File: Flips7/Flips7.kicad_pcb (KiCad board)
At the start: 2 copper layers, 100 x 100 mm, 14 parts, among them U1 FP2800A, U2 FP2800A, U3 FP2800A

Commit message: tracing flips7
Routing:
- net /YR09: track 1.91 -> 128.8 mm, vias 0 -> 1
- net /YR08: track 0.00 -> 123.7 mm, vias 0 -> 1
- net /YS09: track 0.00 -> 118.6 mm, vias 0 -> 2
- net /YS05: track 0.00 -> 118.6 mm, vias 0 -> 1
- net /YS01: track 0.00 -> 116.1 mm, vias 0 -> 1
- net /YS04: track 0.00 -> 115.7 mm, vias 0 -> 1
- net /YR11: track 4.97 -> 120.4 mm, vias 0 -> 1
- net /YS08: track 0.00 -> 113.6 mm, vias 0 -> 1
- net /YS11: track 4.97 -> 115.4 mm, vias 0 -> 1
- net /YS16: track 4.97 -> 105.9 mm, vias 0 -> 3
- net /YS02: track 0.00 -> 98.3 mm, vias 0 -> 1
- net /X01: track 4.97 -> 102.1 mm, vias 0 -> 3
- net /X03: track 4.97 -> 102.1 mm, vias 0 -> 3
- net /X02: track 4.97 -> 101.4 mm, vias 0 -> 3
- net /YR05: track 0.00 -> 95.8 mm, vias 0 -> 1
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- added copper zone on F.Cu, net /X.GND
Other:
- net class Default: via_dia 0.8 -> 0.6; via_drill 0.4 -> 0.3
- net class POW: via_dia 0.8 -> 0.6; via_drill 0.4 -> 0.3

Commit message: adding row driver share connectors
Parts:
- added CN1: Conn_02x16_Odd_Even, Pin_Headers:Pin_Header_Straight_2x16_Pitch2.54mm, F.Cu at (73.0, 57.1)
- added CN2: Conn_02x16_Odd_Even, Pin_Headers:Pin_Header_Straight_2x16_Pitch2.54mm, F.Cu at (125.1, 57.1)
- moved BOARD1 24.1 mm to (77.5, 82.5)
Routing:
- net /YR12: track 67.8 -> 162.1 mm, vias 1 -> 4
- net /YS12: track 56.4 -> 147.2 mm, vias 0 -> 3
- net /YR13: track 65.3 -> 150.7 mm, vias 1 -> 4
- net /YR14: track 75.8 -> 156.0 mm, vias 1 -> 4
- net /YR16: track 79.3 -> 158.9 mm, vias 3 -> 6
- net /YR09: track 128.8 -> 208.4 mm, vias 1 -> 4
- net /YR15: track 79.3 -> 157.7 mm, vias 3 -> 6
- net /YR07: track 55.9 -> 134.2 mm, vias 1 -> 4
- net /YS13: track 62.0 -> 138.8 mm, vias 1 -> 4
- net /YS07: track 62.8 -> 136.3 mm, vias 1 -> 4
- net /YR11: track 120.4 -> 193.8 mm, vias 1 -> 4
- net /YR08: track 123.7 -> 196.9 mm, vias 1 -> 4
- net /YS14: track 93.2 -> 166.2 mm, vias 1 -> 4
- net /YS16: track 105.9 -> 178.3 mm, vias 3 -> 6
- net /YS15: track 95.8 -> 166.9 mm, vias 3 -> 6
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
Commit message: optimize routing
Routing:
- net /YS09: track 187.1 -> 144.6 mm
- net /X02: track 77.6 -> 93.7 mm
- net /X03: track 78.0 -> 90.7 mm
- net /YS16: track 178.3 -> 171.2 mm, vias 6 -> 4
- net /YS15: track 166.9 -> 162.3 mm, vias 6 -> 4
- net /X12: track 57.1 -> 54.0 mm, vias 3 -> 2
- net /YR07: track 134.2 -> 131.1 mm
- net /YR14: track 156.0 -> 154.2 mm
- net /YR13: track 150.7 -> 148.9 mm
- net /YR12: track 162.1 -> 160.3 mm
- net /YR11: track 193.8 -> 192.0 mm
- net /YR09: track 208.4 -> 206.6 mm
- net /YR08: track 196.9 -> 195.1 mm
- net /YR05: track 165.2 -> 163.4 mm
- net /YR04: track 140.4 -> 138.6 mm
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
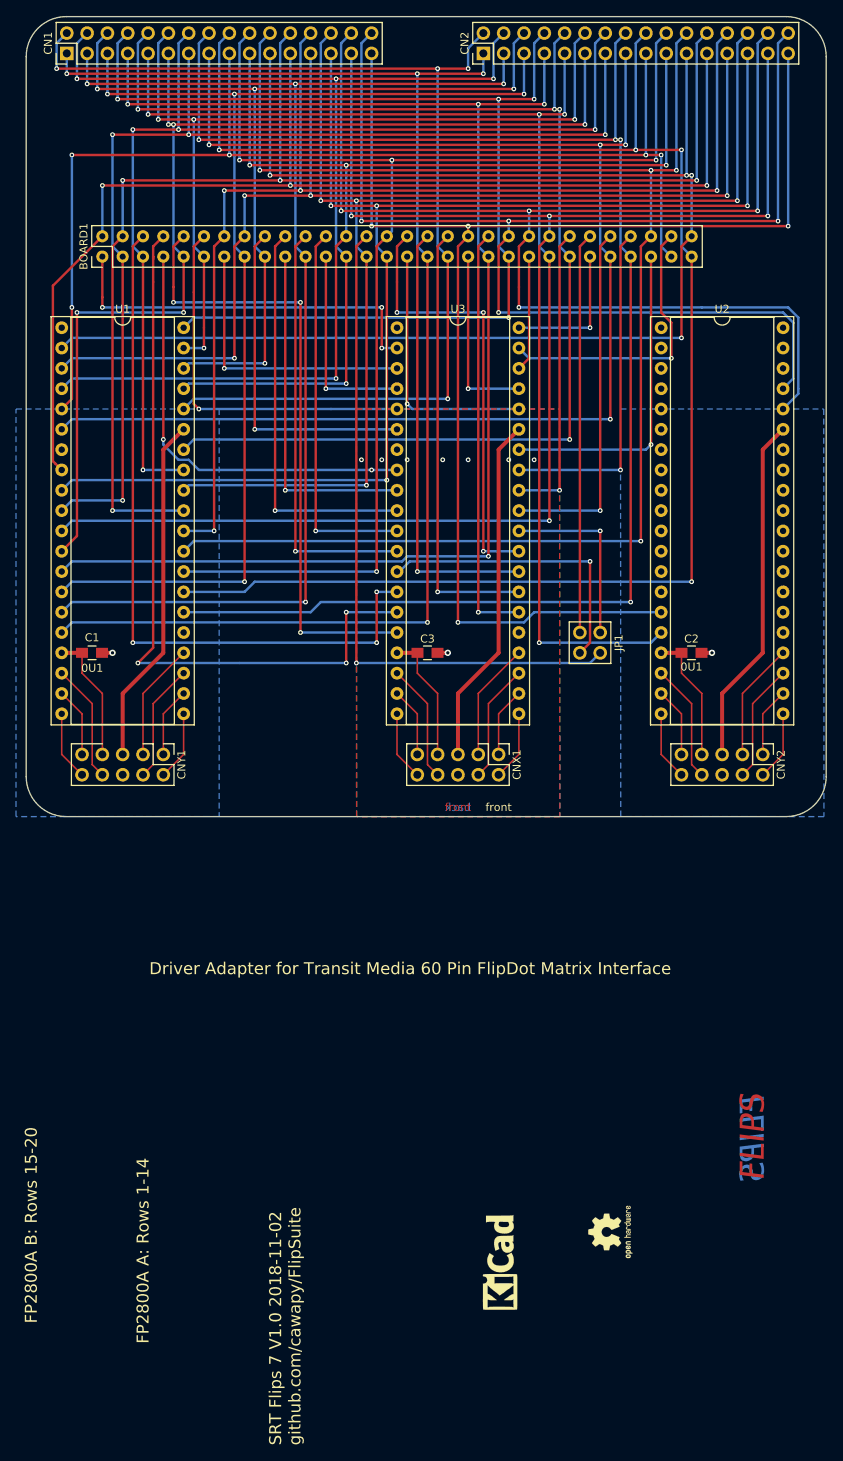
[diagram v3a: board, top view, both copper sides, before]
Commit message: more re-routing
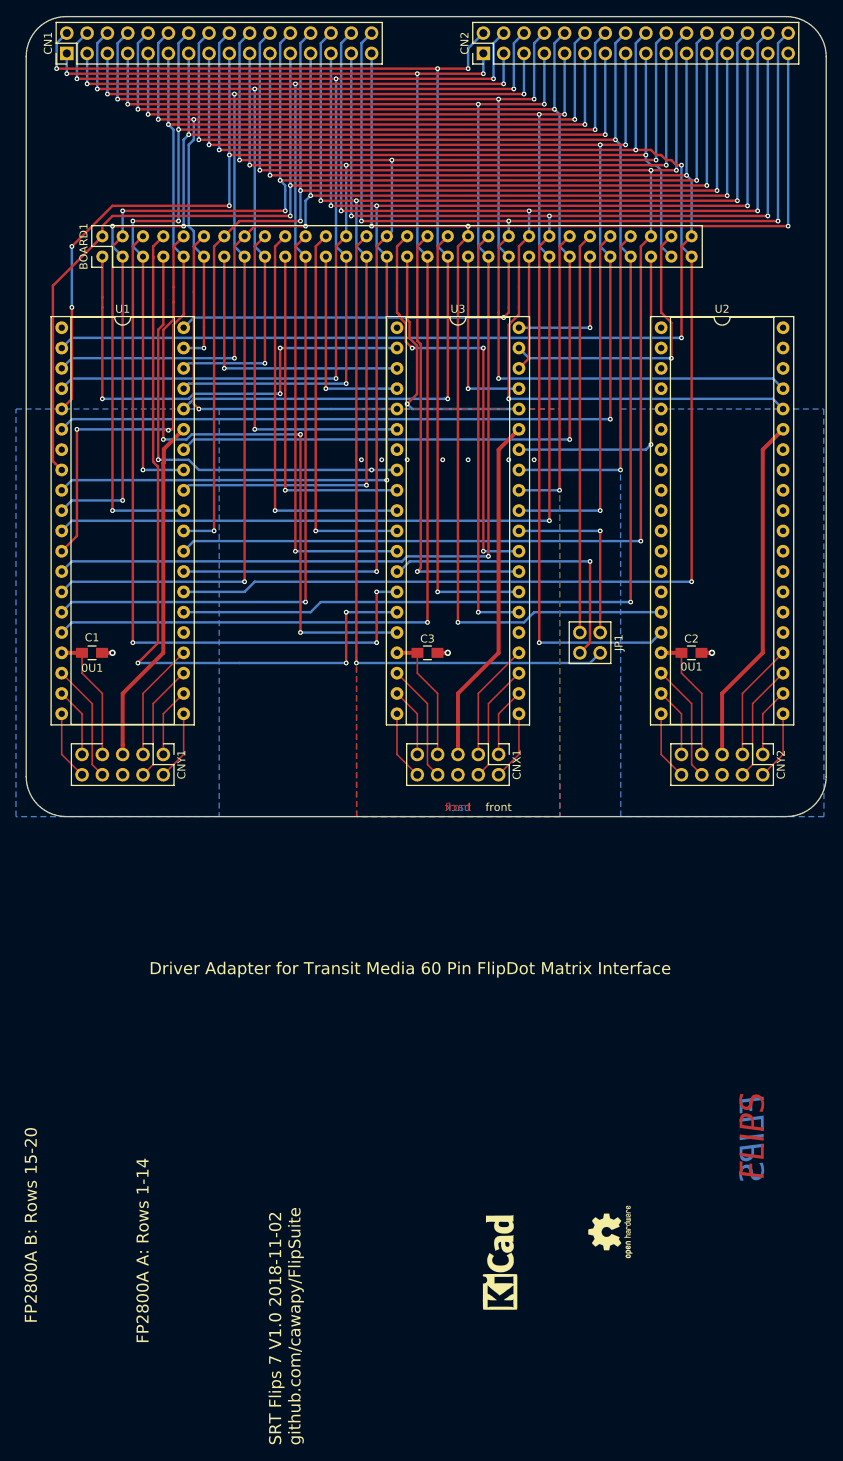
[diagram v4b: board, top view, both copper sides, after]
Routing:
- net /X11: track 48.3 -> 60.6 mm
- net /YS09: track 144.6 -> 140.8 mm
- net /X01: track 78.0 -> 80.7 mm
- net /X12: track 54.0 -> 56.0 mm
- net /YR16: track 158.2 -> 156.4 mm
- net /YS13: track 138.8 -> 137.7 mm
- net /YR09: track 206.6 -> 205.5 mm
- net /X25: track 55.1 -> 54.0 mm
- net /YR13: track 148.9 -> 147.8 mm
- net /X15: track 32.6 -> 33.7 mm
- net /YR15: track 157.8 -> 156.9 mm
- net /YR12: track 160.3 -> 161.2 mm, vias 4 -> 5
- net /YS12: track 147.2 -> 146.4 mm
- net /YR06: track 106.4 -> 106.9 mm
- net /X02: track 93.7 -> 94.2 mm
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
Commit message: rename row pins to /SY## and RY##
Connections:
- net /YR01 renamed /RY01
- net /YR02 renamed /RY02
- net /YR03 renamed /RY03
- net /YR04 renamed /RY04
- net /YR05 renamed /RY05
- net /YR06 renamed /RY06
- net /YR07 renamed /RY07
- net /YR08 renamed /RY08
- net /YR09 renamed /RY09
- net /YR10 renamed /RY10
- net /YR11 renamed /RY11
- net /YR12 renamed /RY12
- net /YR13 renamed /RY13
- net /YR14 renamed /RY14
- net /YR15 renamed /RY15
- net /YR16 renamed /RY16
- net /YS01 renamed /~SY01
- net /YS02 renamed /~SY02
- net /YS03 renamed /~SY03
- net /YS04 renamed /~SY04
- net /YS05 renamed /~SY05
- net /YS06 renamed /~SY06
- net /YS07 renamed /~SY07
- net /YS08 renamed /~SY08
- net /YS09 renamed /~SY09
- net /YS10 renamed /~SY10
- net /YS11 renamed /~SY11
- net /YS12 renamed /~SY12
- net /YS13 renamed /~SY13
- net /YS14 renamed /~SY14
- net /YS15 renamed /~SY15
- net /YS16 renamed /~SY16
